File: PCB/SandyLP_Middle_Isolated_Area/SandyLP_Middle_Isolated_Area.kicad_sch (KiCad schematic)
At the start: 30 parts

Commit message: 基板外形を調整。ネジ位置変更。ゾーンのクリアランス調整。
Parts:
- H1, H2, H3, H4: footprint locallib:MountingHole_1.8-2.2mm_M2_Pad_minimal -> locallib:MountingHole_2.2mm_M2_Pad_minimal
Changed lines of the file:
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@@
 			)
 		)
-		(property "Footprint" "locallib:MountingHole_1.8-2.2mm_M2_Pad_minimal"
+		(property "Footprint" "locallib:MountingHole_2.2mm_M2_Pad_minimal"
 			(at 302.26 172.72 0)
 			(effects
@@
 			)
 		)
-		(property "Footprint" "locallib:MountingHole_1.8-2.2mm_M2_Pad_minimal"
+		(property "Footprint" "locallib:MountingHole_2.2mm_M2_Pad_minimal"
 			(at 302.26 182.88 0)
 			(effects
@@
 			)
 		)
-		(property "Footprint" "locallib:MountingHole_1.8-2.2mm_M2_Pad_minimal"
+		(property "Footprint" "locallib:MountingHole_2.2mm_M2_Pad_minimal"
 			(at 274.32 172.72 0)
 			(effects
@@
 			)
 		)
-		(property "Footprint" "locallib:MountingHole_1.8-2.2mm_M2_Pad_minimal"
+		(property "Footprint" "locallib:MountingHole_2.2mm_M2_Pad_minimal"
 			(at 274.32 182.88 0)
 			(effects

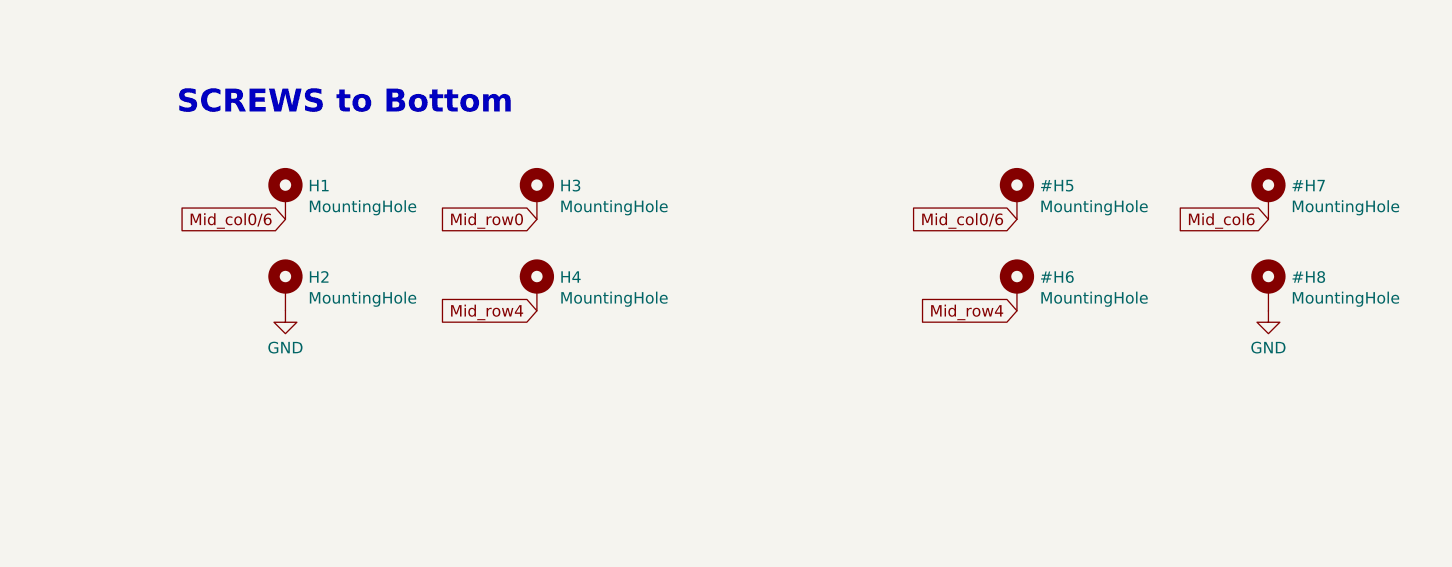
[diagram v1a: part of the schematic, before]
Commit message: USBコネクタ周りの配線に合わせて、Mid孤立部分のネジへのピン割り当てを変更。
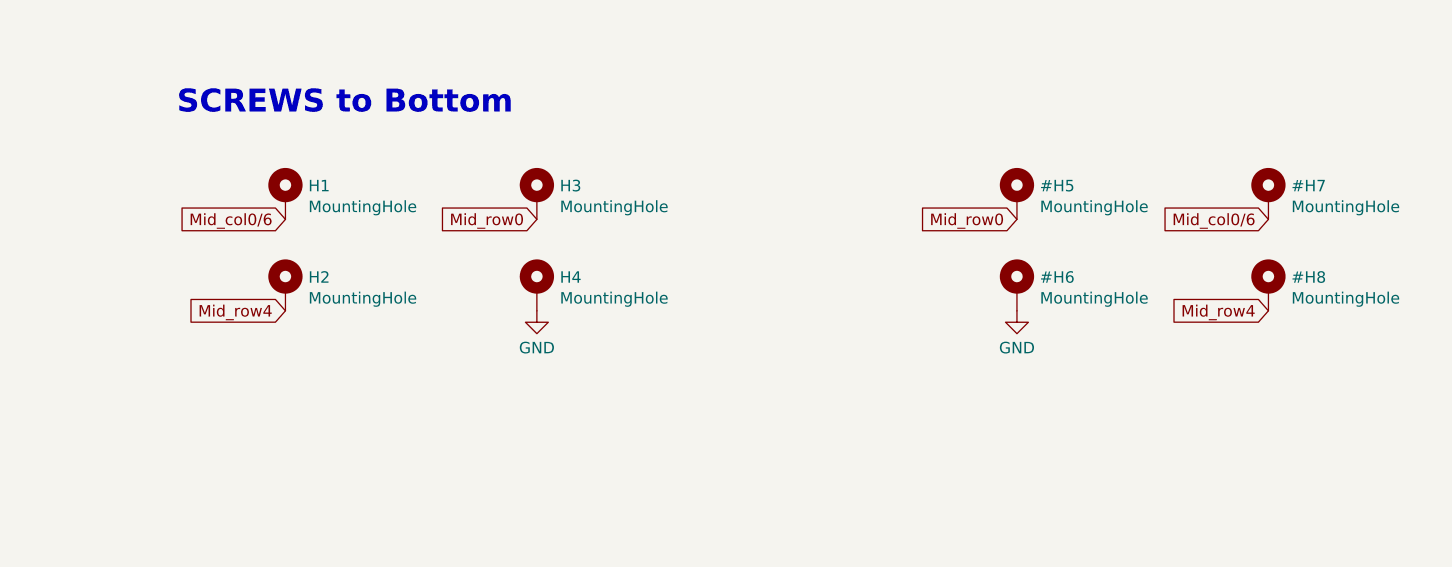
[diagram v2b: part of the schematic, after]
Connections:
- net GND: now also H4.1; no longer H2.1
- net Mid_row4: now also H2.1; no longer H4.1
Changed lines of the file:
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@@
 	(global_label "Mid_row4"
 		(shape input)
-		(at 302.26 185.42 180)
+		(at 274.32 185.42 180)
 		(fields_autoplaced yes)
 		(effects
@@
 		)
 		(property "Intersheetrefs" "${INTERSHEET_REFS}"
-			(at 291.281 185.42 0)
+			(at 263.341 185.42 0)
 			(effects
 				(font
@@
 		)
 		(property "シート間のリファレンス" "${INTERSHEET_REFS}"
-			(at 302.26 187.2552 0)
+			(at 274.32 187.2552 0)
 			(effects
 				(font
@@
 		)
 	)
-	(global_label "Mid_col6"
-		(shape input)
-		(at 383.54 175.26 180)
-		(fields_autoplaced yes)
-		(effects
-			(font
-				(size 1.27 1.27)
-			)
-			(justify right)
-		)
-		(property "Intersheetrefs" "${INTERSHEET_REFS}"
-			(at 372.9239 175.26 0)
-			(effects
-				(font
-					(size 1.27 1.27)
-				)
-				(justify right)
-				(hide yes)
-			)
-		)
-		(property "シート間のリファレンス" "${INTERSHEET_REFS}"
-			(at 383.54 177.0952 0)
-			(effects
-				(font
-					(size 1.27 1.27)
-				)
-				(justify right)
-				(hide yes)
-			)
-		)
-	)
 	(global_label "row3"
 		(shape input)
@@
 	(global_label "Mid_col0{slash}6"
 		(shape input)
-		(at 355.6 175.26 180)
+		(at 383.54 175.26 180)
 		(fields_autoplaced yes)
 		(effects
@@
 		)
 		(property "Intersheetrefs" "${INTERSHEET_REFS}"
-			(at 342.4439 175.26 0)
+			(at 370.3839 175.26 0)
 			(effects
 				(font
@@
 		)
 		(property "シート間のリファレンス" "${INTERSHEET_REFS}"
-			(at 355.6 177.0952 0)
+			(at 383.54 177.0952 0)
 			(effects
 				(font
@@
 	(global_label "Mid_row4"
 		(shape input)
-		(at 355.6 185.42 180)
+		(at 383.54 185.42 180)
 		(fields_autoplaced yes)
 		(effects
@@
 		)
 		(property "Intersheetrefs" "${INTERSHEET_REFS}"
-			(at 344.621 185.42 0)
+			(at 372.561 185.42 0)
 			(effects
 				(font
@@
 		)
 		(property "シート間のリファレンス" "${INTERSHEET_REFS}"
-			(at 355.6 187.2552 0)
+			(at 383.54 187.2552 0)
 			(effects
 				(font
@@
 		)
 	)
+	(global_label "Mid_row0"
+		(shape input)
+		(at 355.6 175.26 180)
+		(fields_autoplaced yes)
+		(effects
+			(font
+				(size 1.27 1.27)
+			)
+			(justify right)
+		)
+		(property "Intersheetrefs" "${INTERSHEET_REFS}"
+			(at 344.621 175.26 0)
+			(effects
+				(font
+					(size 1.27 1.27)
+				)
+				(justify right)
+				(hide yes)
+			)
+		)
+		(property "シート間のリファレンス" "${INTERSHEET_REFS}"
+			(at 355.6 177.0952 0)
+			(effects
+				(font
+					(size 1.27 1.27)
+				)
+				(justify right)
+				(hide yes)
+			)
+		)
+	)
 	(global_label "Mid_row6"
 		(shape input)
@@
 	(symbol
 		(lib_id "power:GND")
-		(at 274.32 185.42 0)
+		(at 302.26 185.42 0)
 		(unit 1)
 		(exclude_from_sim no)
@@
 		(fields_autoplaced yes)
 		(property "Reference" "#PWR05"
-			(at 274.32 191.77 0)
+			(at 302.26 191.77 0)
 			(effects
 				(font
@@
 		)
 		(property "Value" "GND"
-			(at 274.32 189.5531 0)
+			(at 302.26 189.5531 0)
 			(effects
 				(font
@@
 		)
 		(property "Footprint" ""
-			(at 274.32 185.42 0)
+			(at 302.26 185.42 0)
 			(effects
 				(font
@@
 		)
 		(property "Datasheet" ""
-			(at 274.32 185.42 0)
+			(at 302.26 185.42 0)
 			(effects
 				(font
@@
 		)
 		(property "Description" "Power symbol creates a global label with name \"GND\" , ground"
-			(at 274.32 185.42 0)
+			(at 302.26 185.42 0)
 			(effects
 				(font
@@
 	(symbol
 		(lib_id "power:GND")
-		(at 383.54 185.42 0)
+		(at 355.6 185.42 0)
 		(unit 1)
 		(exclude_from_sim no)
@@
 		(fields_autoplaced yes)
 		(property "Reference" "#PWR09"
-			(at 383.54 191.77 0)
+			(at 355.6 191.77 0)
 			(effects
 				(font
@@
 		)
 		(property "Value" "GND"
-			(at 383.54 189.5531 0)
+			(at 355.6 189.5531 0)
 			(effects
 				(font
@@
 		)
 		(property "Footprint" ""
-			(at 383.54 185.42 0)
+			(at 355.6 185.42 0)
 			(effects
 				(font
@@
 		)
 		(property "Datasheet" ""
-			(at 383.54 185.42 0)
+			(at 355.6 185.42 0)
 			(effects
 				(font
@@
 		)
 		(property "Description" "Power symbol creates a global label with name \"GND\" , ground"
-			(at 383.54 185.42 0)
+			(at 355.6 185.42 0)
 			(effects
 				(font

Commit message: ネジとソケットのパッドか近くはんだ付けが心配なため、パッドを少し小さくする。
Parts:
- SW_TAB1: footprint locallib:Kailh_socket_ChocV2_for_Reverse -> locallib:Kailh_socket_ChocV2_for_Reverse_narrow_#2pad
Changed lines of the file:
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@@
 			)
 		)
-		(property "Footprint" "locallib:Kailh_socket_ChocV2_for_Reverse"
+		(property "Footprint" "locallib:Kailh_socket_ChocV2_for_Reverse_narrow_#2pad"
 			(at 43.18 40.005 0)
 			(effects
